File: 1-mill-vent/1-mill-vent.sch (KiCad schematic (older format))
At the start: 60 parts, among them J1 Differential:/Single, J3 No_Power_Control, J4 Front_panel_control, J5 Fan, J6 Ext Parts, J7 EXT Power Option, J8 POWER, Q1 2N3904, Q2 2N3904, Q3 2N3904, Q4 TSM480p06, U1 LM358, U2 LM78L05_TO92, U3 TSR_1-24120, U4 MPXV

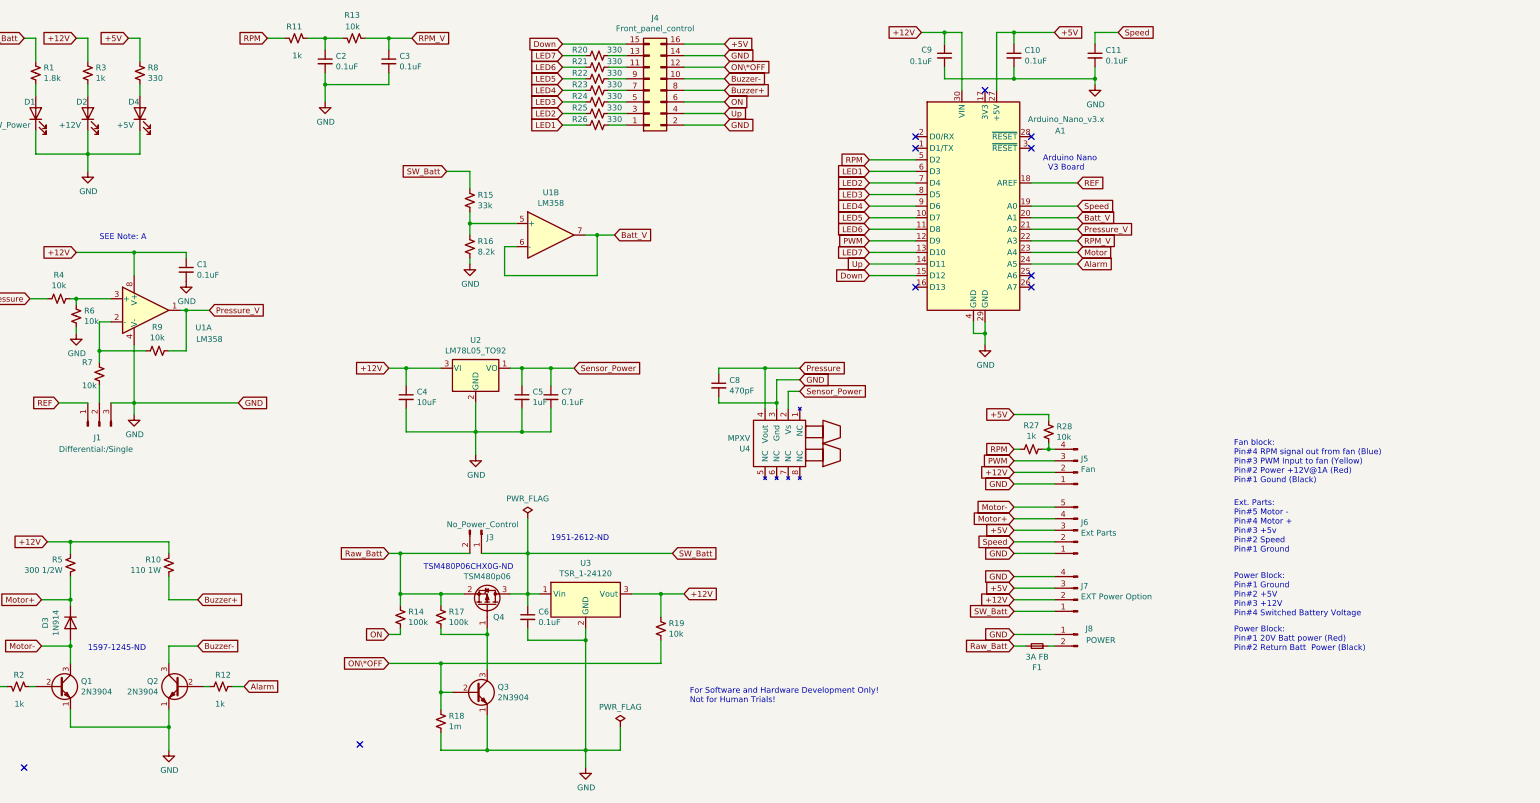
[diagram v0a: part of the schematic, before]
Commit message: Last update to ver1, start v2
V1 is first board
V2 is start of SMD design
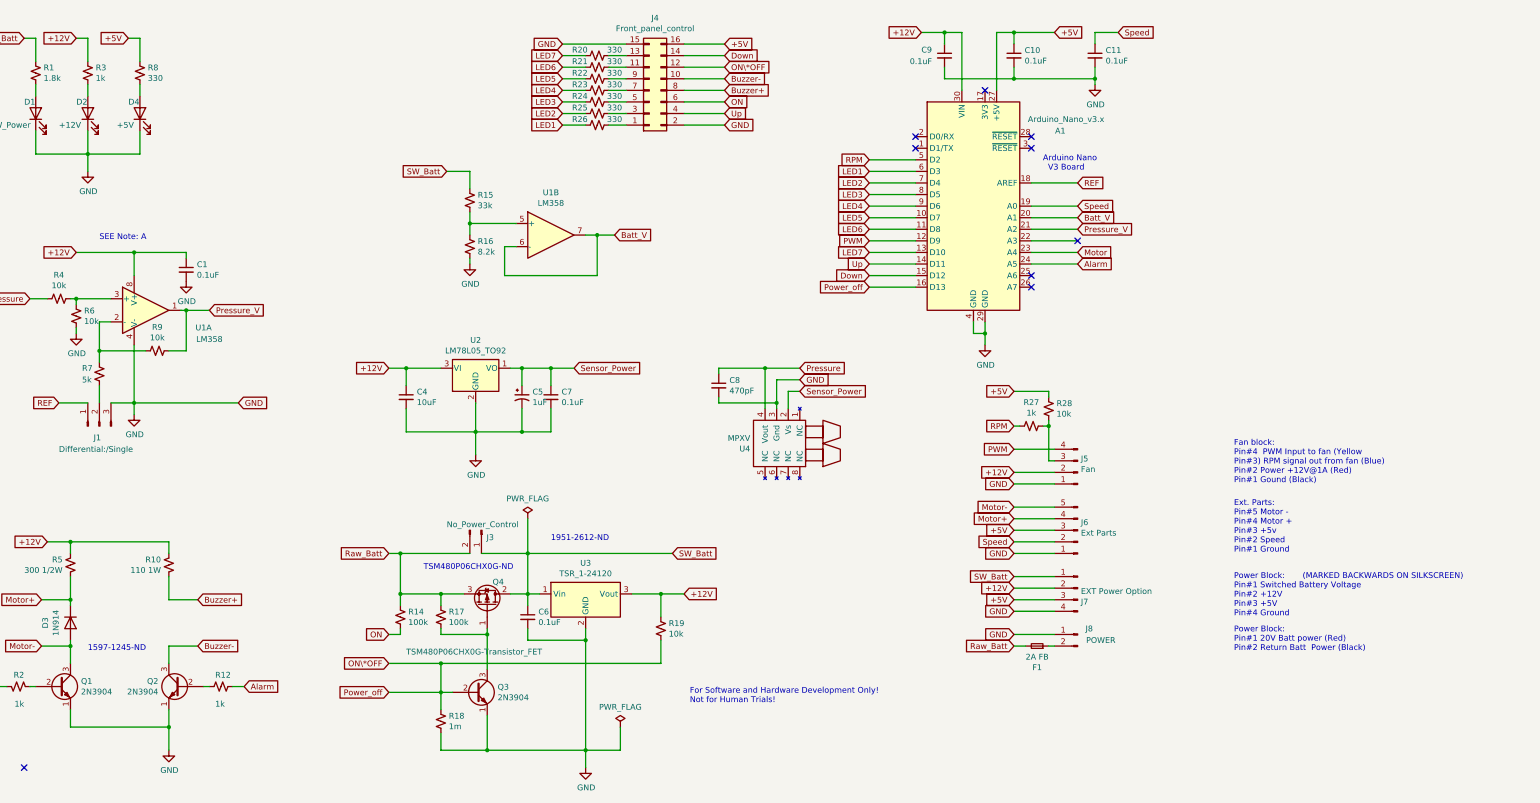
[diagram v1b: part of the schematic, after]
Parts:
- removed C2, C3: 0.1uF, Capacitor_THT:C_Axial_L3.8mm_D2.6mm_P7.50mm_Horizontal, symbol Device:C_Small
- removed C5: 1uF, Capacitor_THT:C_Axial_L3.8mm_D2.6mm_P12.50mm_Horizontal, symbol Device:C_Small
- removed Q4: TSM480p06, Package_TO_SOT_THT:TO-251-3_Vertical, symbol 1-mill-vent-rescue:TSM2301ACX-Transistor_FET
- removed R11: 1k, Resistor_THT:R_Axial_DIN0207_L6.3mm_D2.5mm_P2.54mm_Vertical, symbol Device:R_Small_US
- removed R13: 10k, Resistor_THT:R_Axial_DIN0207_L6.3mm_D2.5mm_P2.54mm_Vertical, symbol Device:R_Small_US
- added C5: 1uF, Capacitor_THT:CP_Radial_Tantal_D5.5mm_P2.50mm, symbol Device:CP1_Small
- added Q4: TSM480P06CHX0G-Transistor_FET, Package_TO_SOT_THT:TO-251-3_Vertical, symbol 1-mill-vent-rescue:TSM480P06CHX0G-Transistor_FET
- C1, C10, C11, C6, C7, C9: footprint Capacitor_THT:C_Axial_L3.8mm_D2.6mm_P7.50mm_Horizontal -> Capacitor_THT:C_Rect_L7.2mm_W2.5mm_P5.00mm_FKS2_FKP2_MKS2_MKP2
- C4, C8: footprint Capacitor_THT:C_Axial_L3.8mm_D2.6mm_P12.50mm_Horizontal -> Capacitor_THT:C_Rect_L7.0mm_W3.5mm_P5.00mm
- F1: value 3A FB -> 2A FB
- R7: value 10k -> 5k
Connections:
- net Down: now also J4.14 (Pin_14); no longer J4.15 (Pin_15)
- net GND: now also J4.15 (Pin_15), C5.2; no longer J4.14 (Pin_14)
- net ON\*OFF: now also A1.16 (D13)
- net PWM: now also J5.4 (Pin_4); no longer J5.3 (Pin_3)
- net Raw_Batt: now also Q4.3 (S)
- net SW_Batt: now also Q4.2 (D)
- net Sensor_Power: now also C5.1
- net at Q3.3 (C), R17.2: now also Q4.1 (G)
- net at R27.2, R28.1: now also J5.3 (Pin_3); no longer J5.4 (Pin_4)
- net RPM_V: no longer names the net of A1.22 (A3)
- no-connect marks 10 -> 9
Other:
- note added: "Fan block:\nPin#4 PWM Input to fan (Yellow\nPin#3) RPM signal out from fan (Blue)\nPin#2 Power +12V@1A (Red)\nPin#1 Gound (Black)"
- note added: "Power Block: (MARKED BACKWARDS ON SILKSCREEN)\nPin#1 Switched Battery Voltage\nPin#2 +12V\nPin#3 +5V\nPin#4 Ground"
- note removed: "Fan block:\nPin#4 RPM signal out from fan (Blue)\nPin#3 PWM Input to fan (Yellow)\nPin#2 Power +12V@1A (Red)\nPin#1 Gound (Black)"
- note removed: "Power Block:\nPin#1 Ground\nPin#2 +5V\nPin#3 +12V\nPin#4 Switched Battery Voltage"
- moved on the sheet: R27, R28
